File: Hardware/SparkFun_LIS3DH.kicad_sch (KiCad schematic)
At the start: 25 parts, among them J3 Qwiic_RA, J4 I2C, J5 Qwiic_RA, U1 VEML7700-TT

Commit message: Makes some changes to the main IC
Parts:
- removed U1: VEML7700-TT, SparkFun-Sensor:VEML7700-TT, symbol SparkFun-Sensor:VEML7700-TT
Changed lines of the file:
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@@
-	)
-	(symbol
-		(lib_id "SparkFun-Sensor:VEML7700-TT")
-		(at 96.52 59.69 0)
-		(unit 1)
-		(exclude_from_sim no)
-		(in_bom yes)
-		(on_board yes)
-		(dnp no)
-		(fields_autoplaced yes)
-		(property "Reference" "U1"
-			(at 96.52 49.53 0)
-			(effects
-				(font
-					(size 1.27 1.27)
-				)
-			)
-		)
-		(property "Value" "VEML7700-TT"
-			(at 96.52 52.07 0)
-			(effects
-				(font
-					(size 1.27 1.27)
-				)
-			)
-		)
-		(property "Footprint" "SparkFun-Sensor:VEML7700-TT"
-			(at 96.52 70.104 0)
-			(effects
-				(font
-					(size 1.27 1.27)
-				)
-				(hide yes)
-			)
-		)
-		(property "Datasheet" "https://www.vishay.com/docs/84286/veml7700.pdf"
-			(at 96.266 73.152 0)
-			(effects
-				(font
-					(size 1.27 1.27)
-				)
-				(hide yes)
-			)
-		)
-		(property "Description" "VEML7700 is a high accuracy ambient light digital 16-bit resolution sensor in a miniature transparent 6.8 mm x 2.35 mm x 3.0 mm package."
-			(at 95.504 76.708 0)
-			(effects
-				(font
-					(size 1.27 1.27)
-				)
-				(hide yes)
-			)
-		)
-		(property "PROD_ID" "IC-16311"
-			(at 96.52 78.232 0)
-			(effects
-				(font
-					(size 1.27 1.27)
-				)
-				(hide yes)
-			)
-		)
-		(pin "1"
-		)
-		(pin "3"
-		)
-		(pin "2"
-		)
-		(pin "4"
-		)
-		(instances
-			(project ""
-				(path "/e3dd3ae4-244d-4cba-9cca-5d2abf83f29a"
-					(reference "U1")
-					(unit 1)
-				)
-			)
-		)
 	)
 	(symbol

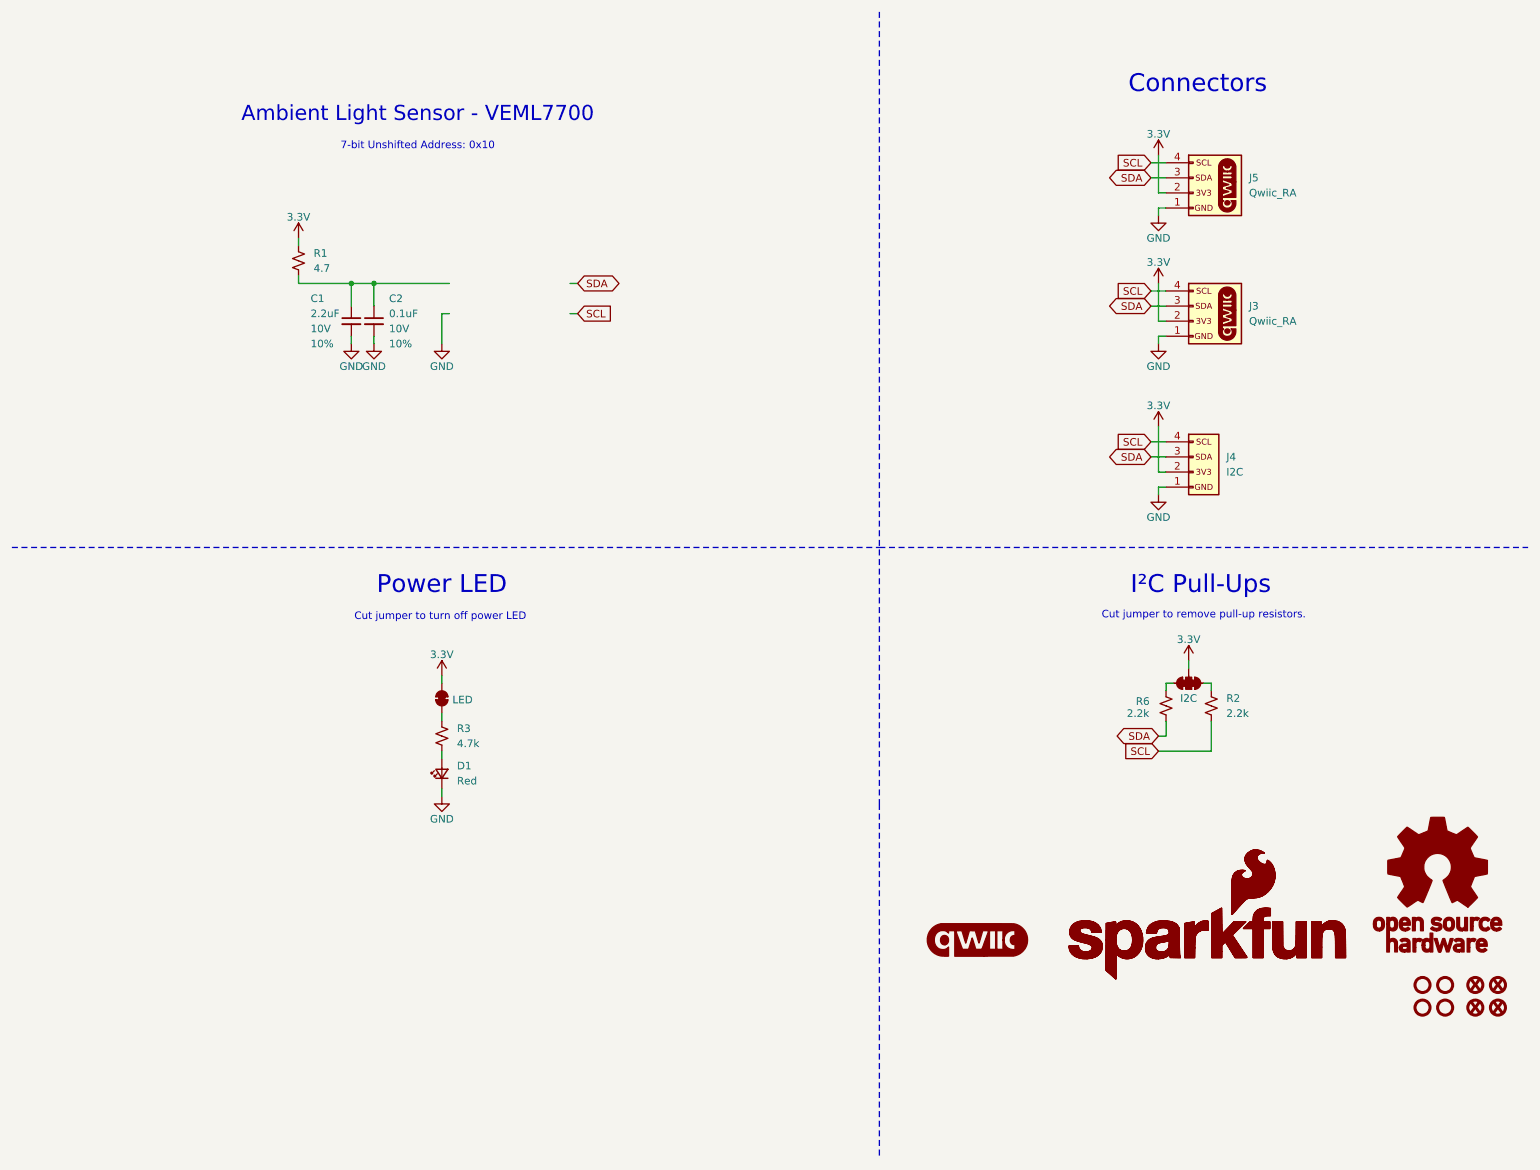
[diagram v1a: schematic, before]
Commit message: Adds the new LIS3DH symbol and footprint to schematic and PCB
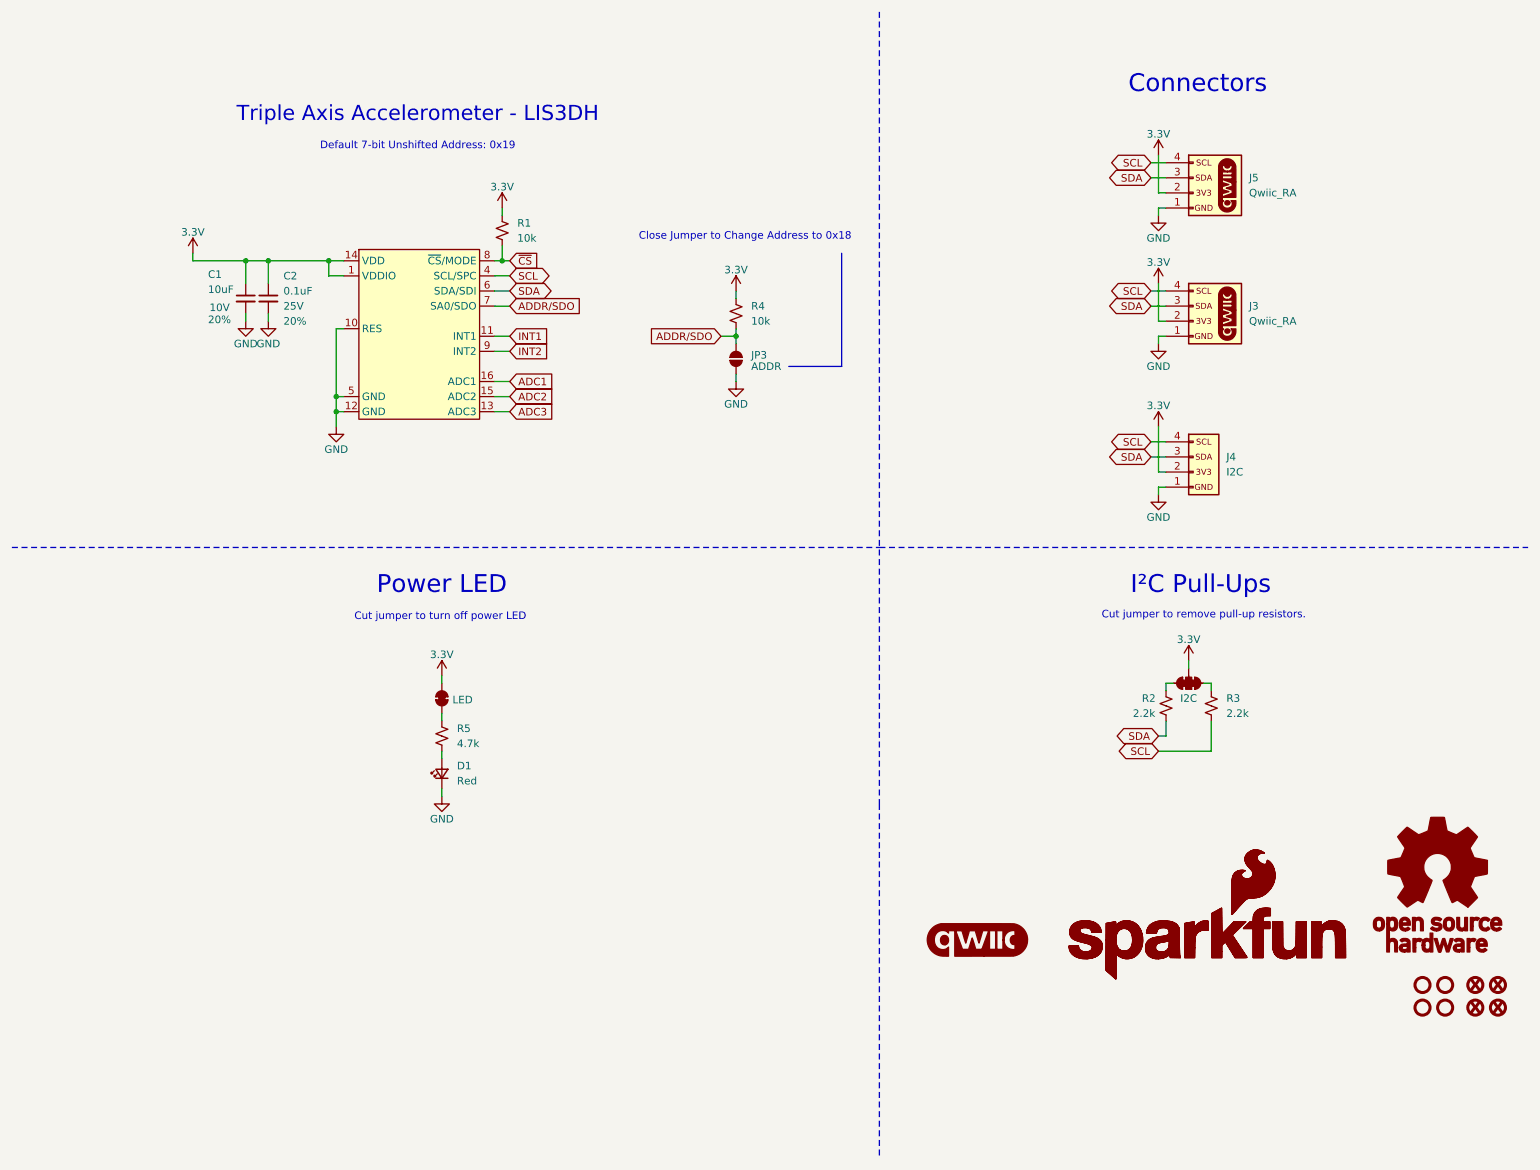
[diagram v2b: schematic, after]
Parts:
- removed C1: 2.2uF, SparkFun-Capacitor:C_0402_1005Metric, symbol SparkFun-Capacitor:2.2uF_0402_10V_10%
- removed C2: 0.1uF, SparkFun-Capacitor:C_0402_1005Metric, symbol SparkFun-Capacitor:0.1uF_0402_10V_10%
- removed R1: 4.7, SparkFun-Resistor:R_0402_1005Metric, symbol SparkFun-Resistor:4.7_0402
- removed R2, R6: 2.2k, SparkFun-Resistor:R_0402_1005Metric, symbol SparkFun-Resistor:2.2k_0402
- removed R3: 4.7k, SparkFun-Resistor:R_0402_1005Metric, symbol SparkFun-Resistor:4.7k_0402
- added C1: 10uF, SparkFun-Capacitor:C_0603_1608Metric, symbol SparkFun-Capacitor:10uF_0603_10V_20%
- added C2: 0.1uF, SparkFun-Capacitor:C_0603_1608Metric, symbol SparkFun-Capacitor:0.1uF_0603_25V_20%
- added JP3: ADDR, SparkFun-Jumper:Jumper_2_NO, symbol SparkFun-Jumper:SolderJumper_2_Open
- added R1, R4: 10k, SparkFun-Resistor:R_0603_1608Metric, symbol SparkFun-Resistor:10k_0603
- added R2, R3: 2.2k, SparkFun-Resistor:R_0603_1608Metric, symbol SparkFun-Resistor:2.2k_0603
- added R5: 4.7k, SparkFun-Resistor:R_0603_1608Metric, symbol SparkFun-Resistor:4.7k_0603
- added U1: LIS3DH, SparkFun-Sensor:LGA-16-3X3, symbol SparkFun-Sensor:LIS3DH
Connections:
- net 3.3V: now also C1.1, C2.1, R1.2, R4.2, U1.1 (VDDIO), U1.14 (VDD)
- net GND: now also C1.2, C2.2, JP3.1 (A), U1.10 (RES), U1.12 (GND), U1.5 (GND)
- net SCL: now also R3.1, U1.4 (SCL/SPC)
- net SDA: now also R2.1, U1.6 (SDA/SDI)
- net at D1.2 (A): now also R5.1
- net at JP1.1 (A): now also R5.2
- net at JP2.1 (A): now also R3.2
- net at JP2.3 (C): now also R2.2
- new net ADC1: U1.16 (ADC1)
- new net ADC2: U1.15 (ADC2)
- new net ADC3: U1.13 (ADC3)
- new net ADDR/SDO: JP3.2 (B), R4.1, U1.7 (SA0/SDO)
- new net INT1: U1.11 (INT1)
- new net INT2: U1.9 (INT2)
- new net ~{CS}: R1.1, U1.8 (~{CS}/MODE)
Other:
- note added: "Close Jumper to Change Address to 0x18"
- note added: "Default 7-bit Unshifted Address: 0x19"
- note added: "Triple Axis Accelerometer - LIS3DH"
- note removed: "7-bit Unshifted Address: 0x10"
- note removed: "Ambient Light Sensor - VEML7700"

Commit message: Adds silks, moves components arounds
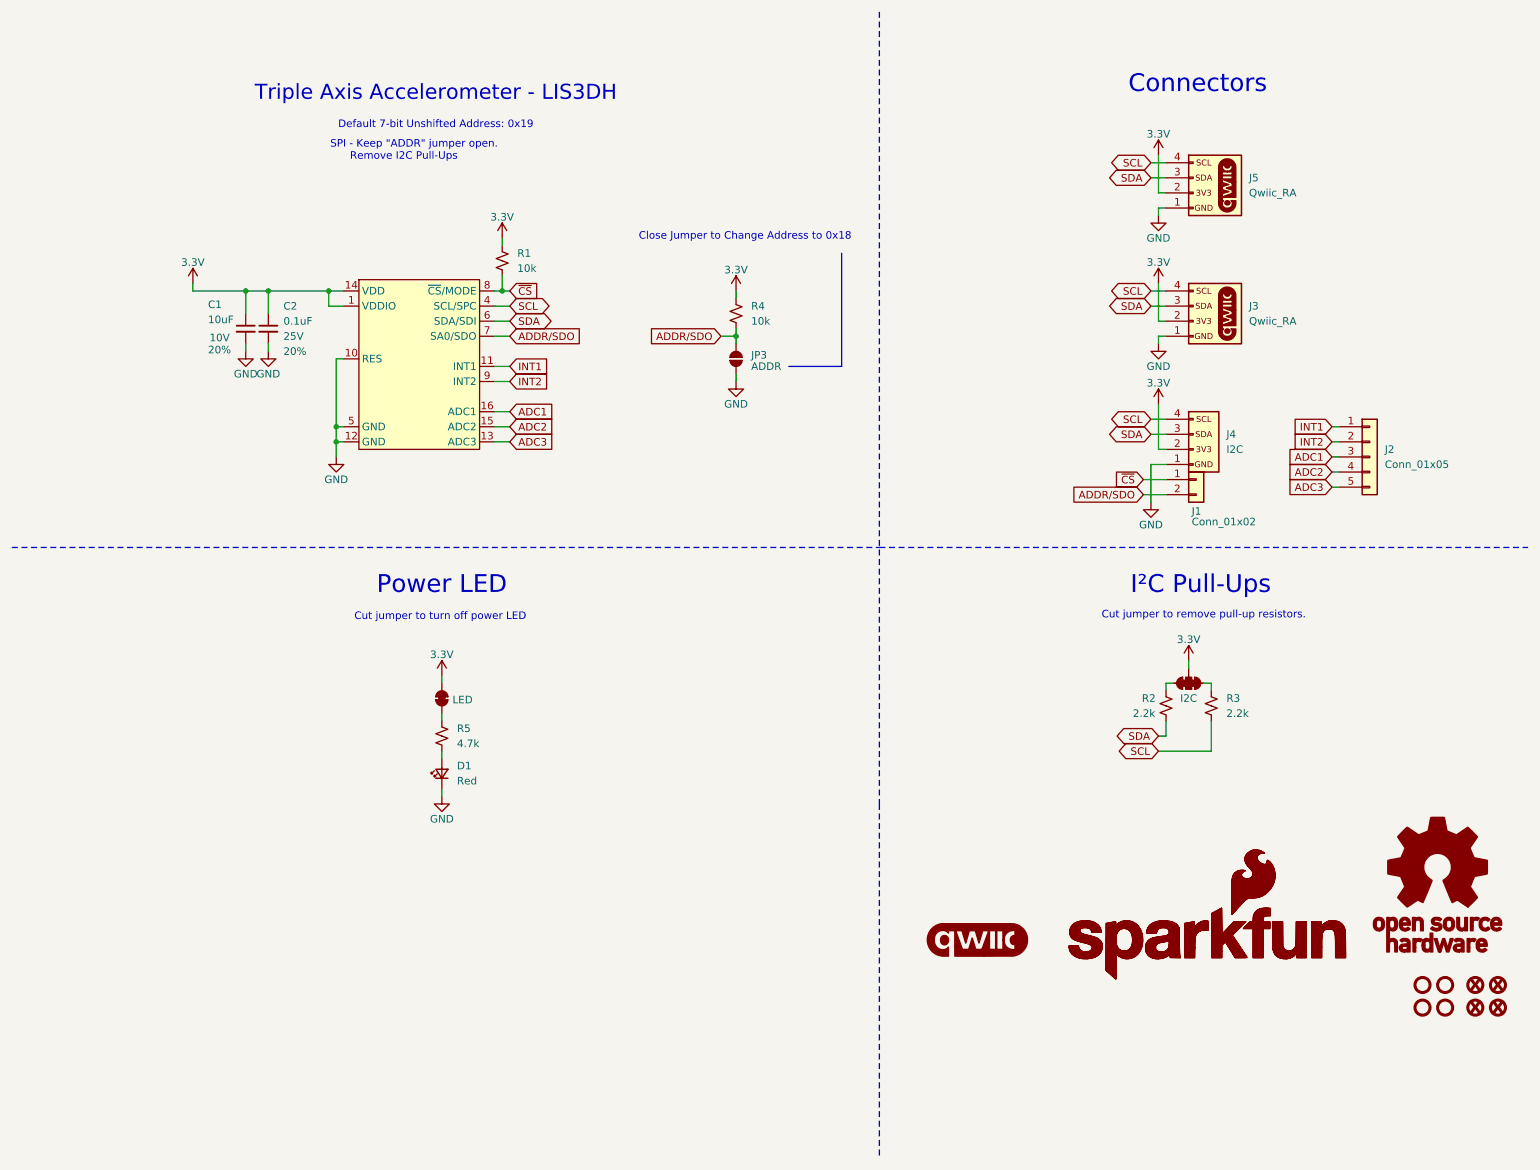
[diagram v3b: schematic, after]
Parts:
- added J1: Conn_01x02, SparkFun-Connector:1x02, symbol SparkFun-Connector:Conn_01x02
- added J2: Conn_01x05, SparkFun-Connector:1x05, symbol SparkFun-Connector:Conn_01x05
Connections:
- net ADC1: now also J2.3 (Pin_3)
- net ADC2: now also J2.4 (Pin_4)
- net ADC3: now also J2.5 (Pin_5)
- net ADDR/SDO: now also J1.2 (Pin_2)
- net INT1: now also J2.1 (Pin_1)
- net INT2: now also J2.2 (Pin_2)
- net ~{CS}: now also J1.1 (Pin_1)
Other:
- note added: "SPI - Keep "ADDR" jumper open. Remove I2C Pull-Ups"
- moved on the sheet: C1, C2, J4, R1

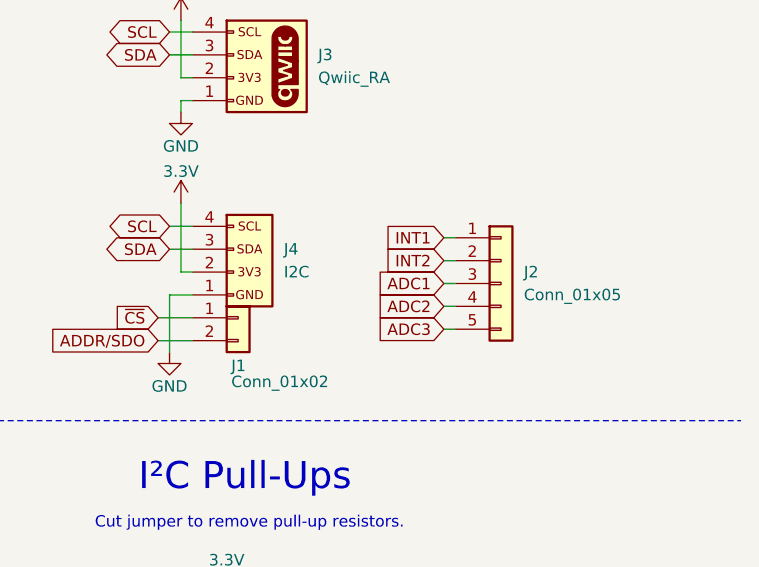
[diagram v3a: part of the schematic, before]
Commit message: Adjust routing, adds keepout underneath sensor, moves clock out from underneath IC
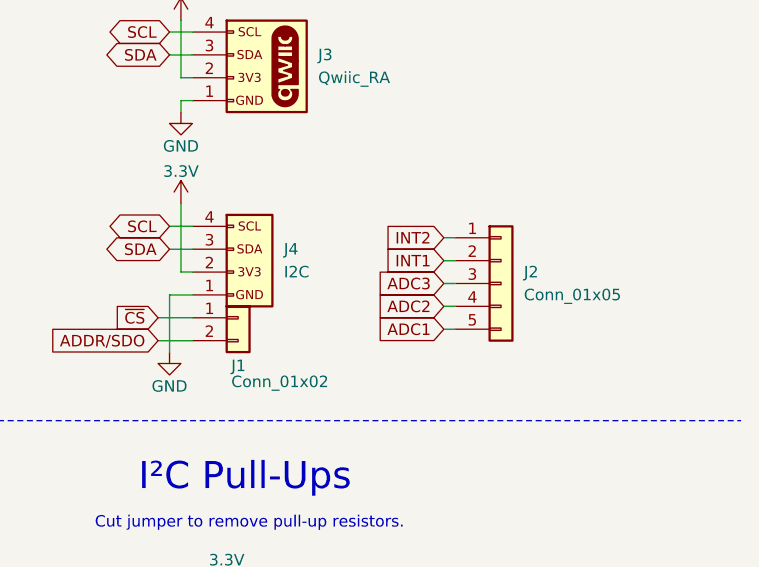
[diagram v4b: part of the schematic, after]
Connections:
- net ADC1: now also J2.5 (Pin_5); no longer J2.3 (Pin_3)
- net ADC3: now also J2.3 (Pin_3); no longer J2.5 (Pin_5)
- net INT1: now also J2.2 (Pin_2); no longer J2.1 (Pin_1)
- net INT2: now also J2.1 (Pin_1); no longer J2.2 (Pin_2)
